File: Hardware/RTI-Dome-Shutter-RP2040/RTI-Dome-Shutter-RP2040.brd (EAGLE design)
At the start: 99.7 x 76.3 mm, 65 parts, among them IC2 24LC64T-I/SN, IC4 RASPBERRY_PI_PICO, IC8 REG1117-3.3V, IC9 REG1117-5V, J2 XT60PW-M

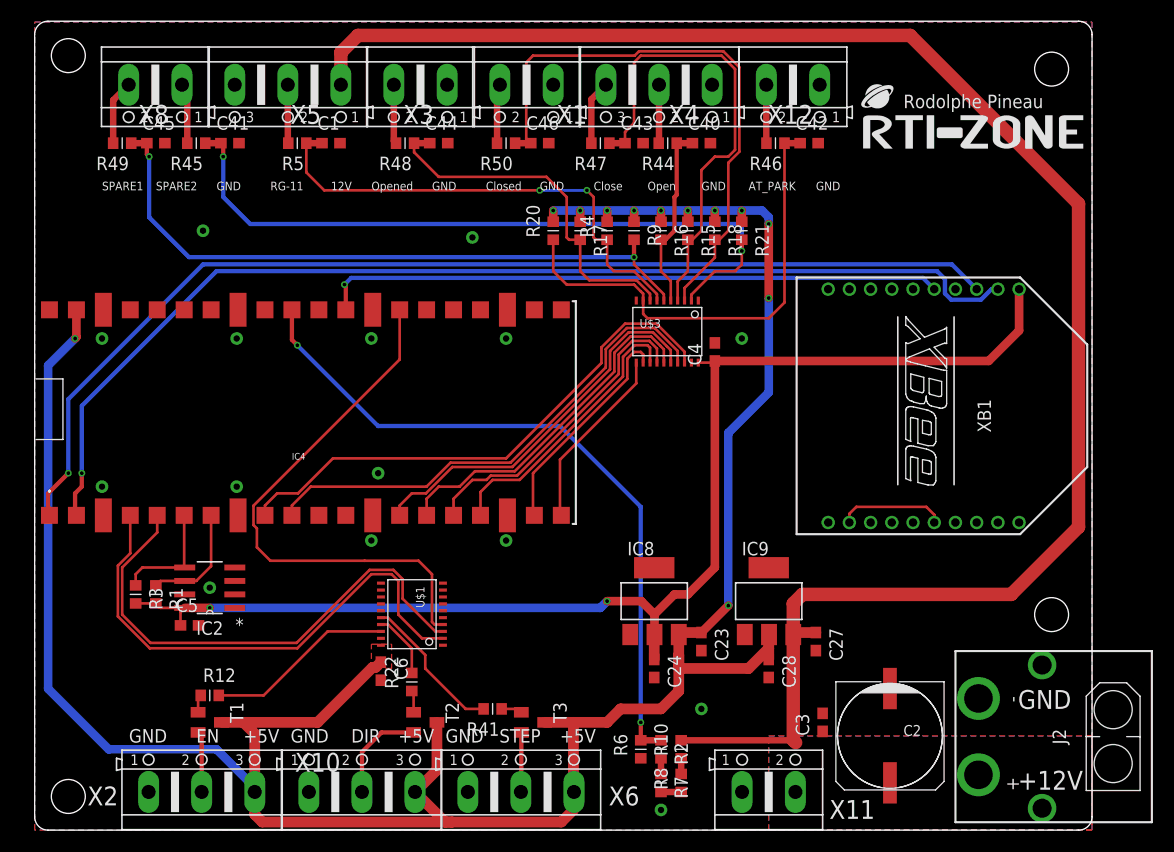
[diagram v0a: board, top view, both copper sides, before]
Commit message: Removed XBee from RP2040 Shutter controller
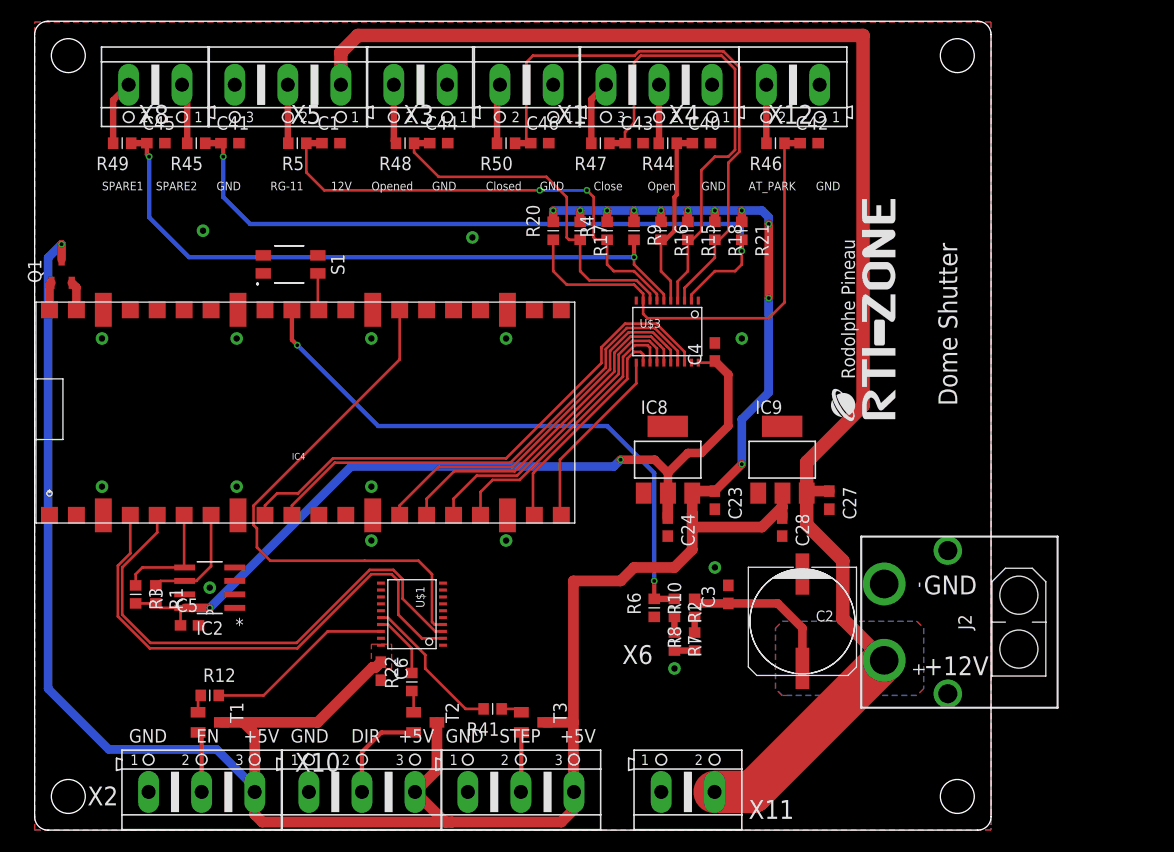
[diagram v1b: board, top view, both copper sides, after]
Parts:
- removed XB1: XBEE, rti:XBEE
- added Q1: DMG2305UX-7, samacsys:SOT96P240X115-3N
- added S1: EVQ-P2H02B, samacsys:EVQP2H02B
- IC4: value RASPBERRY_PI_PICO -> RASPBERRY_PI_PICOW; device samacsys:RASPBERRYPIPICO -> samacsys:RASPBERRYPIPICO-W
- moved U$4 25.7 mm to (81.2, 38.7), turned to 90 degrees
- moved C3 15.0 mm to (65.4, 22.2)
- moved J2 14.0 mm to (80.1, 19.6)
- moved C2 13.6 mm to (72.4, 19.7)
- moved C23 13.4 mm to (64.1, 31.1)
- moved C27 13.4 mm to (74.9, 31.1)
- moved R2 13.4 mm to (60.3, 21.0)
- moved R6 13.4 mm to (58.4, 21.0)
- moved R7 13.4 mm to (60.3, 17.8)
- moved R8 13.4 mm to (62.2, 17.8)
- moved C24 13.4 mm to (59.7, 28.6)
- moved C28 13.4 mm to (70.5, 28.6)
- moved IC8 13.4 mm to (59.7, 34.9)
- moved IC9 13.4 mm to (70.5, 34.9)
- moved R10 13.4 mm to (62.2, 21.0)
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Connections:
- removed net N$64: IC4.40
- removed net N$9: XB1.12, XB1.16
- new net VBUS: IC4.40, Q1.1
- new net VSYS: IC4.39, Q1.2
- net 3.3V: no longer XB1.1
- net GND: now also S1.2, S1.4; no longer XB1.10, XB1.9
- net RESET: now also S1.3
- net VCC: now also Q1.3; no longer IC4.39
- net XBEE_DIN: no longer XB1.3
- net XBEE_DOUT: no longer XB1.2
- net XBEE_RESET: no longer XB1.5
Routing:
- net XBEE_DOUT: track 104.6 -> 0.00 mm, vias 1 -> 0
- net XBEE_DIN: track 103.7 -> 0.00 mm, vias 1 -> 0
- net XBEE_RESET: track 58.7 -> 0.00 mm, vias 1 -> 0
- net 3.3V: track 118.3 -> 78.6 mm
- net +12V: track 166.2 -> 155.5 mm
- net VPIN: track 66.2 -> 56.0 mm
- net N$9: track 10.1 -> 0.00 mm
- net VCC: track 243.3 -> 251.1 mm
- net RESET: track 0.00 -> 3.47 mm
- net VSYS: track 0.00 -> 2.73 mm
- net VBUS: track 0.00 -> 2.62 mm
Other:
- board size 99.7 x 76.3 mm -> 90.2 x 76.3 mm

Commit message: Removed XBee from RP2040 boards as they'll use WiFi
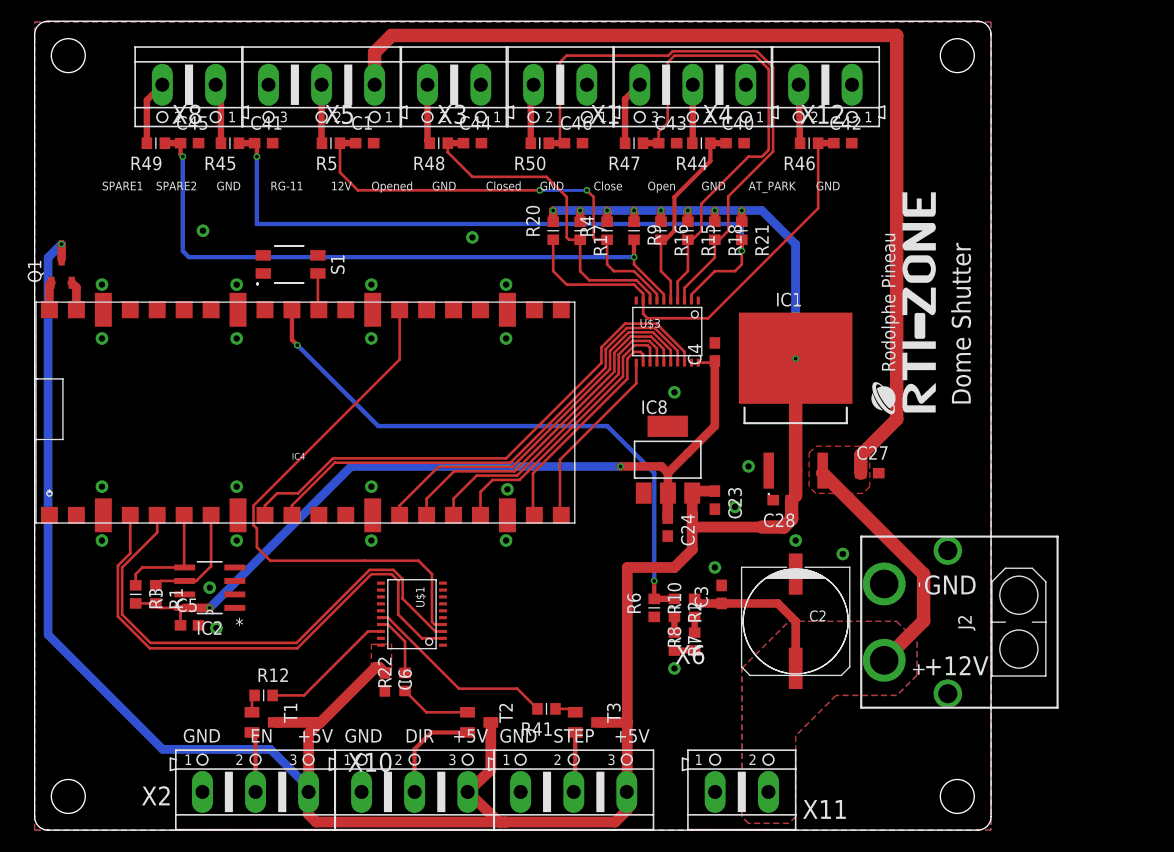
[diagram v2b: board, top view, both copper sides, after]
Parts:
- removed IC9: REG1117-5V, burr-brown:SOT223
- added IC1: REG1117FA-5.0_500, REG1117FA-5.0_500:REG1117FA50500
- moved X2 5.08 mm to (20.8, 3.60)
- moved R12 5.08 mm to (21.6, 12.7)
- moved R41 5.08 mm to (48.3, 11.4)
- moved T1 5.08 mm to (21.6, 10.2)
- moved T2 5.08 mm to (41.9, 10.2)
- moved T3 5.08 mm to (52.1, 10.2)
- moved X11 5.08 mm to (66.7, 3.60)
- moved X6 4.98 mm to (50.8, 3.60)
- moved X10 4.97 mm to (35.8, 3.60)
- moved C27 4.58 mm to (78.7, 33.7), turned to 0 degrees
- moved U$4 3.86 mm to (85.0, 39.4)
- moved X4 3.19 mm to (62.1, 70.3)
- moved X5 3.18 mm to (27.1, 70.3)
- moved R46 3.18 mm to (73.0, 64.8)
- moved C40 3.18 mm to (66.0, 64.8)
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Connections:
- net +12V: now also IC1.3; no longer IC9.3
- net GND: now also IC1.1; no longer IC9.1
- net VCC: now also IC1.2, IC1.4; no longer IC9.2
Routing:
- net +12V: track 155.5 -> 133.6 mm
- net VCC: track 251.1 -> 244.2 mm, vias 12 -> 10
- net M_EN_5V: track 17.8 -> 12.7 mm
- net DIR-5V_TR: track 2.08 -> 6.72 mm
- net M_STEP_5V: track 14.0 -> 18.3 mm
- net SHUTTER_OPENED_IN_5V: track 34.7 -> 31.5 mm
- net RG-11-IN_5V: track 46.2 -> 43.1 mm
- net 3.3V: track 78.6 -> 76.2 mm
- net AT_PARK_PIN_IN_5V: track 44.8 -> 42.8 mm
- net SPARE1_IN_5V: track 67.9 -> 66.3 mm
- net SPARE2_IN_5V: track 62.8 -> 61.5 mm
- net BUTTON_WEST_CLOSE_IN_5V: track 44.8 -> 46.1 mm
- net BUTTON_EAST_OPEN_5V: track 17.6 -> 18.9 mm
- net HOME_SHUTTER_CLOSED_IN_5V: track 54.8 -> 56.1 mm
